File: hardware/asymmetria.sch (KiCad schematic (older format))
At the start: 36 parts, among them P1 CONN_01X02, P2 CONN_01X03, P3 CONN_01X02, P5 CONN_01X02, SW1 3x6x2.5mm, SW2 3x6x2.5mm, U1 AMS1117-3.3, U2 PT4115B89E, U3 ESP8266EX, U4 W25Q32FV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

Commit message: component checks
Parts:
- added W1, W2: MH, Connect:1pin, symbol TEST_1P
- SW1, SW2: footprint Buttons_Switches_SMD:SW_SPST_EVQPE1 -> umetronics:SPST_3x6x2.5_SMD
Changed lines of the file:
@@
 F 0 "SW1" H 950 5910 50  0000 C CNN
 F 1 "3x6x2.5mm" H 800 5720 50  0000 C CNN
-F 2 "Buttons_Switches_SMD:SW_SPST_EVQPE1" H 800 5800 60  0001 C CNN
+F 2 "umetronics:SPST_3x6x2.5_SMD" H 800 5800 60  0001 C CNN
 F 3 "" H 800 5800 60  0000 C CNN
 	1    800  5800
@@
 F 0 "SW2" H 1800 5910 50  0000 C CNN
 F 1 "3x6x2.5mm" H 1650 5720 50  0000 C CNN
-F 2 "Buttons_Switches_SMD:SW_SPST_EVQPE1" H 1650 5800 60  0001 C CNN
+F 2 "umetronics:SPST_3x6x2.5_SMD" H 1650 5800 60  0001 C CNN
 F 3 "" H 1650 5800 60  0000 C CNN
 	1    1650 5800
@@
 Wire Wire Line
 	4450 2700 4650 2700
+$Comp
+L TEST_1P W1
+U 1 1 566187EA
+P 2250 7400
+F 0 "W1" H 2250 7670 50  0000 C CNN
+F 1 "MH" H 2250 7600 50  0000 C CNN
+F 2 "Connect:1pin" H 2450 7400 50  0001 C CNN
+F 3 "" H 2450 7400 50  0000 C CNN
+	1    2250 7400
+	1    0    0    -1
+$EndComp
+$Comp
+L TEST_1P W2
+U 1 1 5661895C
+P 2450 7400
+F 0 "W2" H 2450 7670 50  0000 C CNN
+F 1 "MH" H 2450 7600 50  0000 C CNN
+F 2 "Connect:1pin" H 2650 7400 50  0001 C CNN
+F 3 "" H 2650 7400 50  0000 C CNN
+	1    2450 7400
+	1    0    0    -1
+$EndComp
 $EndSCHEMATC

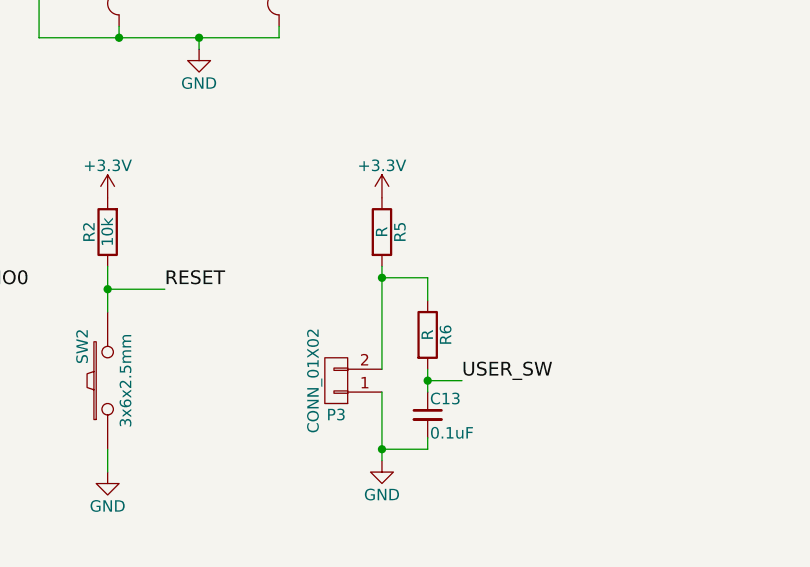
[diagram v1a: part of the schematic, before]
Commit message: added debounce resistor values
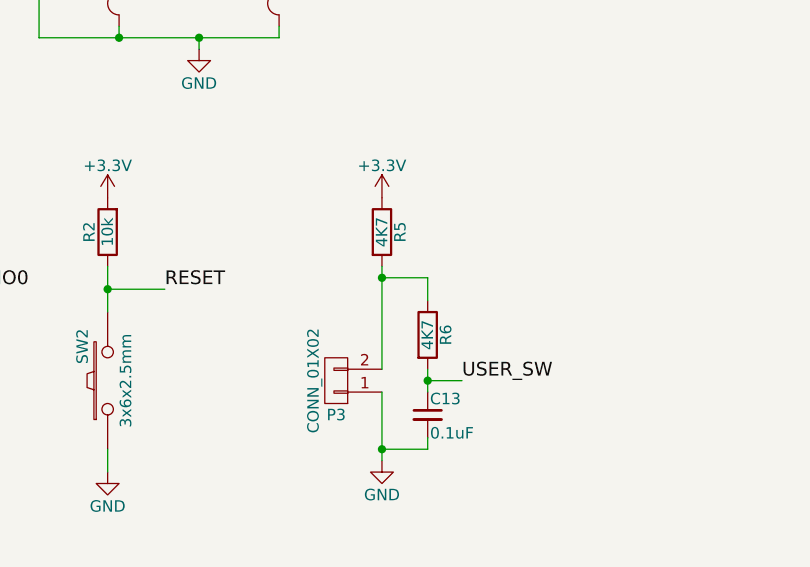
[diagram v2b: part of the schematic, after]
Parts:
- R5, R6: value R -> 4K7
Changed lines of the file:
@@
 P 2850 5150
 F 0 "R5" V 2930 5150 50  0000 C CNN
-F 1 "R" V 2850 5150 50  0000 C CNN
+F 1 "4K7" V 2850 5150 50  0000 C CNN
 F 2 "Resistors_SMD:R_0603" V 2780 5150 30  0001 C CNN
 F 3 "" H 2850 5150 30  0000 C CNN
@@
 P 3050 5600
 F 0 "R6" V 3130 5600 50  0000 C CNN
-F 1 "R" V 3050 5600 50  0000 C CNN
+F 1 "4K7" V 3050 5600 50  0000 C CNN
 F 2 "Resistors_SMD:R_0603" V 2980 5600 30  0001 C CNN
 F 3 "" H 3050 5600 30  0000 C CNN

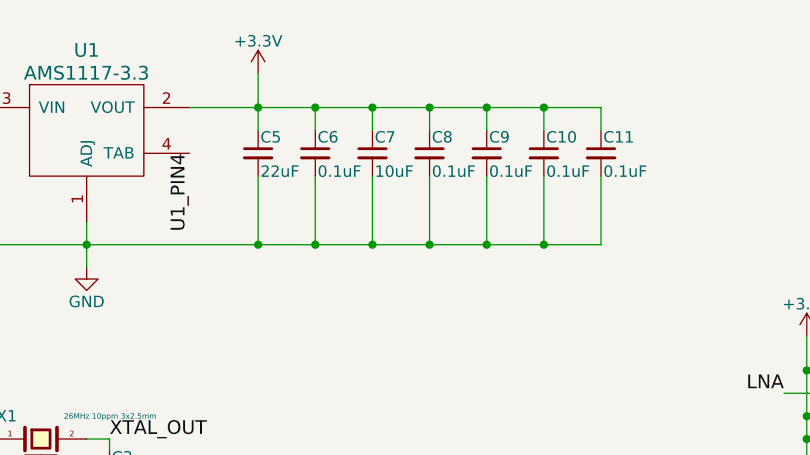
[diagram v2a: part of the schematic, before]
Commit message: grounded qfn center pad, increased C7 to 100uF
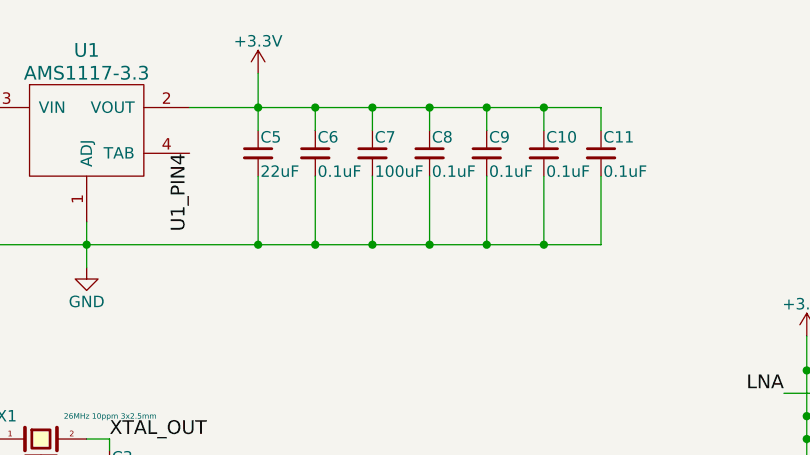
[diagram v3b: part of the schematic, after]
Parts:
- C7: value 10uF -> 100uF
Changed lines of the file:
@@
 P 2650 1250
 F 0 "C7" H 2660 1320 50  0000 L CNN
-F 1 "10uF" H 2660 1170 50  0000 L CNN
+F 1 "100uF" H 2660 1170 50  0000 L CNN
 F 2 "Capacitors_SMD:C_1206" H 2650 1250 60  0001 C CNN
 F 3 "" H 2650 1250 60  0000 C CNN

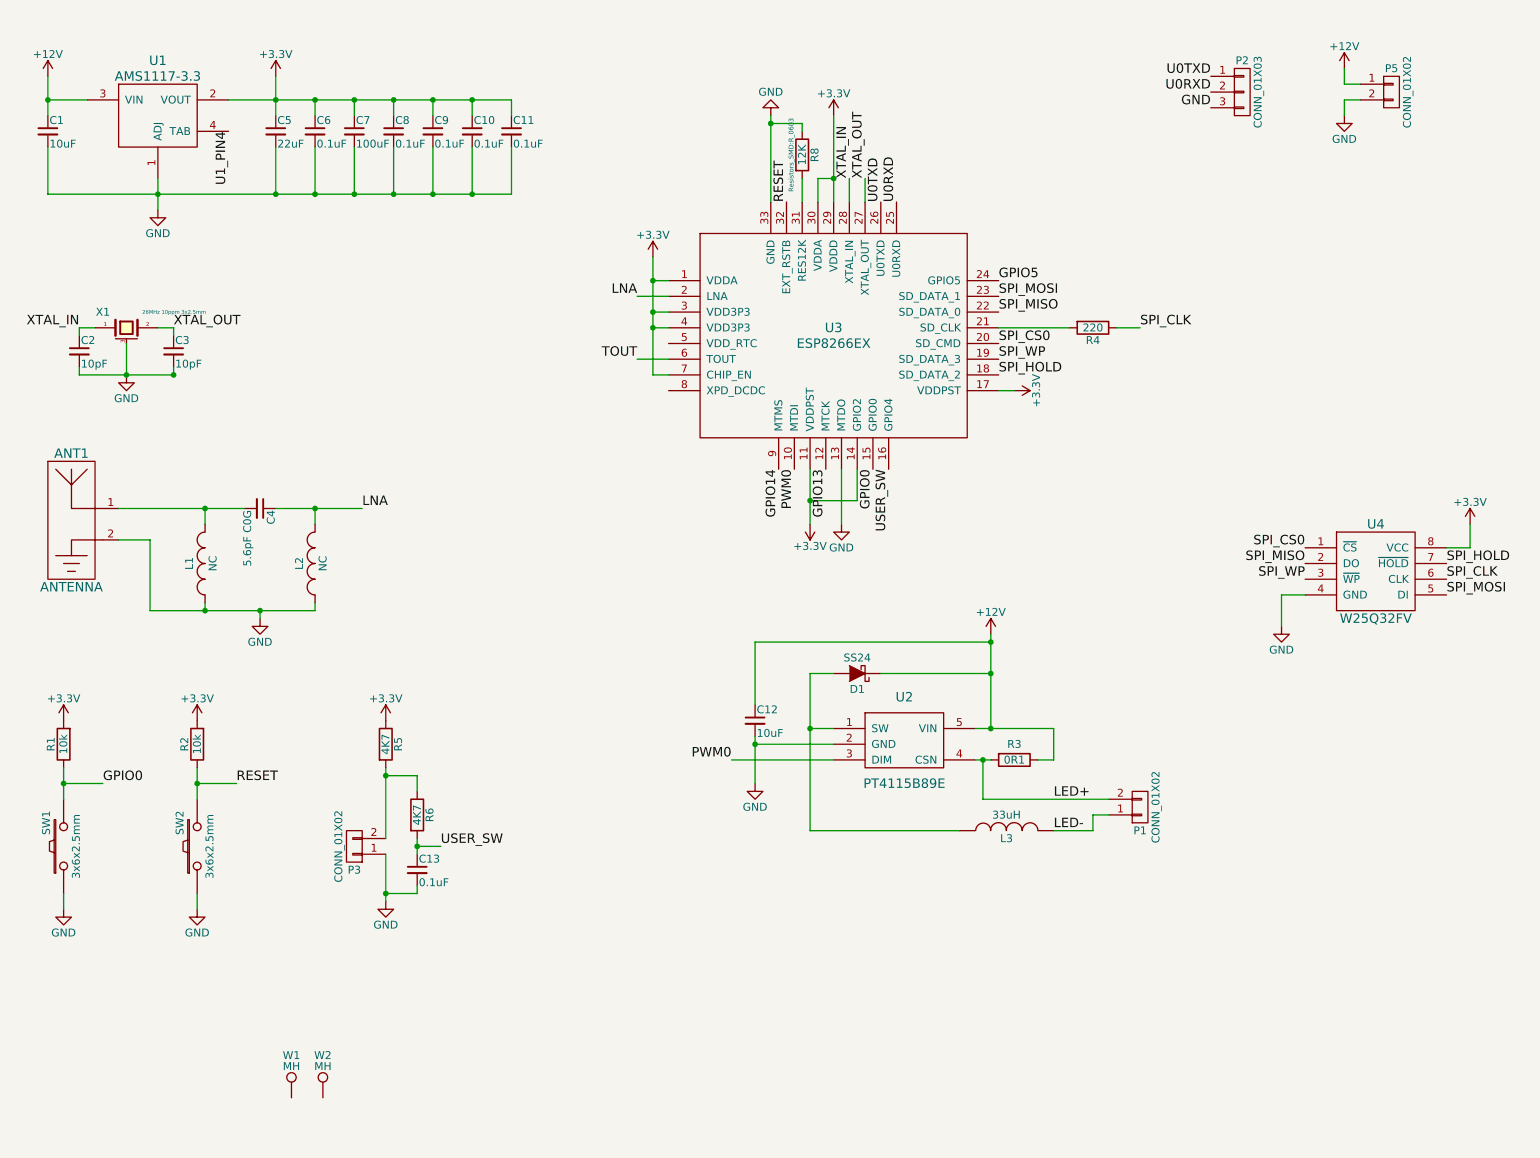
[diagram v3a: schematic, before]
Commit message: group schematic into sections
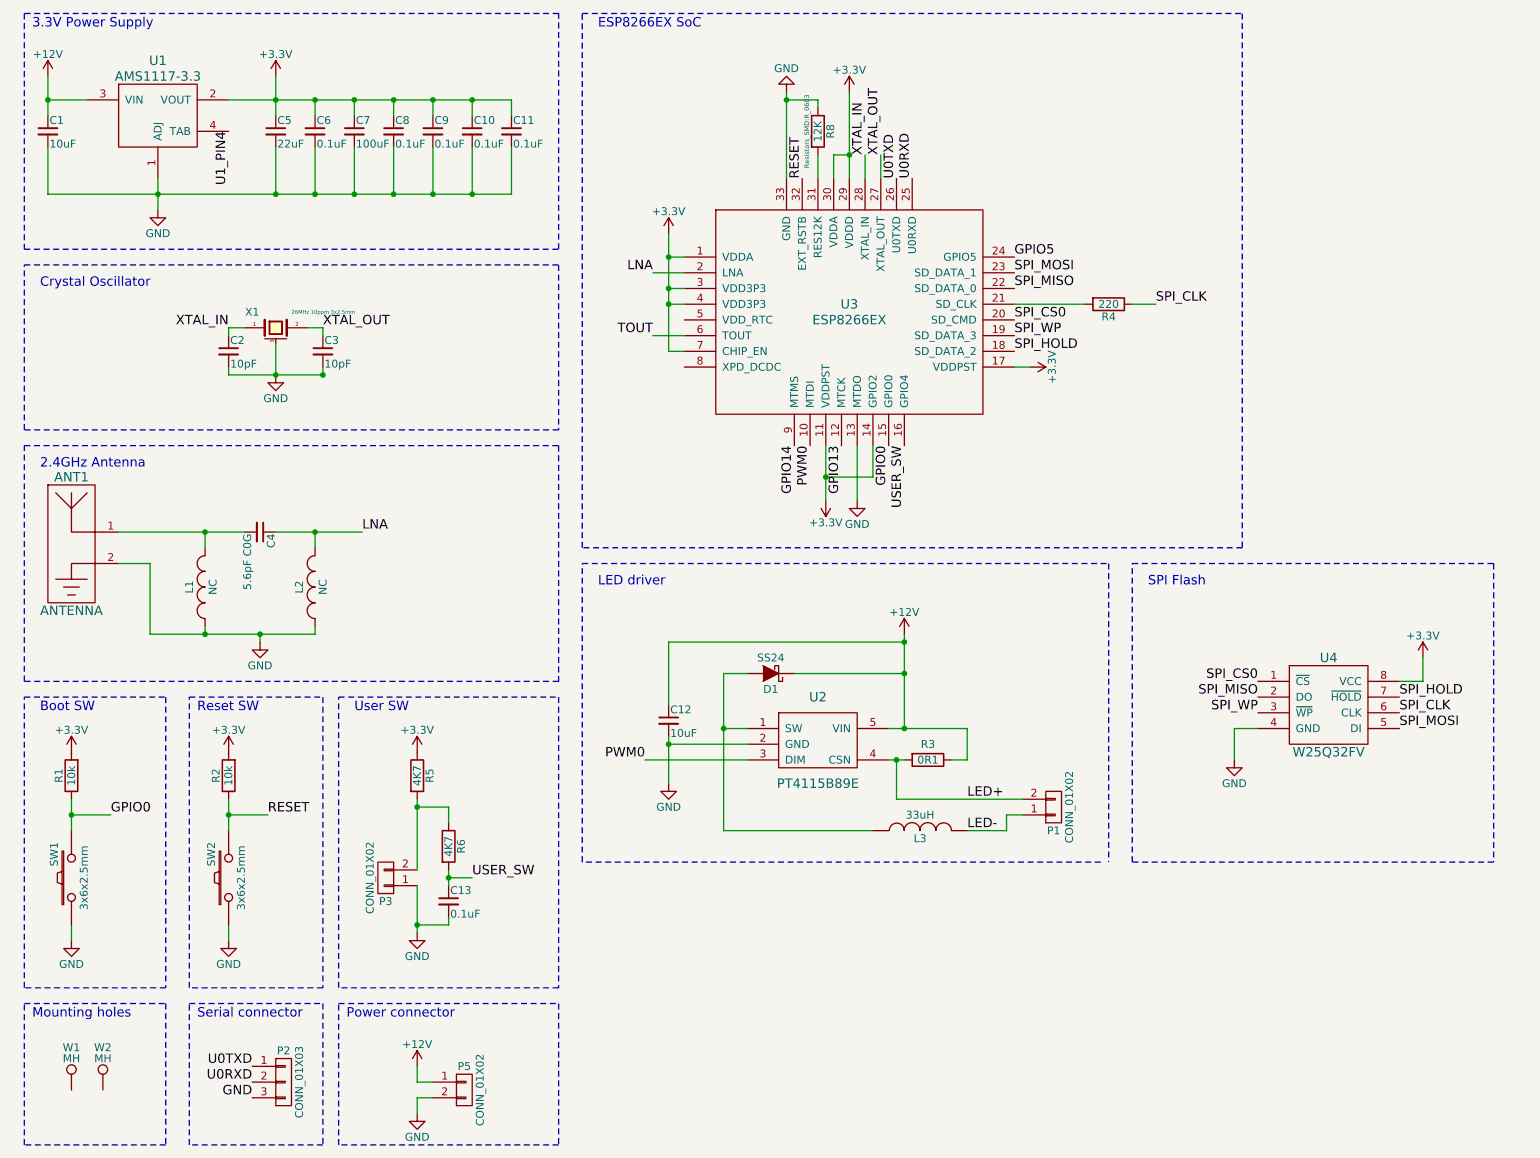
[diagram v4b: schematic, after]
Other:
- note added: "2.4GHz Antenna"
- note added: "3.3V Power Supply"
- note added: "Boot SW"
- note added: "Crystal Oscillator"
- note added: "ESP8266EX SoC"
- note added: "LED driver"
- note added: "Mounting holes"
- note added: "Power connector"
- note added: "Reset SW"
- note added: "SPI Flash"
- note added: "Serial connector"
- note added: "User SW"
- moved on the sheet: ANT1, C12, C13, C2, C3, C4, D1, L1, L2, L3, P1, P2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
